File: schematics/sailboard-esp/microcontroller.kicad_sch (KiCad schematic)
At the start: 2 parts

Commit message: v1.1 of sailboard.
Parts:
- removed LOGICTRANS1: TXB0108DQSR, Package_SON:USON-20_2x4mm_P0.4mm, symbol Logic_LevelTranslator:TXB0108DQSR
- added LEVEL_TRANSLATE1: TXB0108PWR, SOP65P640X120-20N, symbol TXB0108PWR:TXB0108PWR
- ESP32: footprint MODULE_ESP32-DEVKITC -> ESP32-DEVKITC:MODULE_ESP32-DEVKITC-RESIZED
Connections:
- net +3.3V: now also LEVEL_TRANSLATE1.10 (OE), LEVEL_TRANSLATE1.2 (VCCA)
- net +5V: now also LEVEL_TRANSLATE1.19 (VCCB)
- net GND: now also LEVEL_TRANSLATE1.11 (GND)
- net PROP_ENABLE_1_5V: now also LEVEL_TRANSLATE1.18 (B2)
- net PROP_ENABLE_2_5V: now also LEVEL_TRANSLATE1.20 (B1)
- net PROP_PWM_5V: now also LEVEL_TRANSLATE1.17 (B3)
- net RADIO_CHAN1_5V: now also LEVEL_TRANSLATE1.15 (B5)
- net RADIO_CHAN2_5V: now also LEVEL_TRANSLATE1.14 (B6)
- net RUDDER_PWM_5V: now also LEVEL_TRANSLATE1.16 (B4)
- net at ESP32.28 (IO17): now also LEVEL_TRANSLATE1.1 (A1)
- net at ESP32.27 (IO16): now also LEVEL_TRANSLATE1.3 (A2)
- net at ESP32.26 (IO4): now also LEVEL_TRANSLATE1.4 (A3)
- net at ESP32.25 (IO0): now also LEVEL_TRANSLATE1.5 (A4)
- net at ESP32.24 (IO2): now also LEVEL_TRANSLATE1.6 (A5)
- net at ESP32.23 (IO15): now also LEVEL_TRANSLATE1.7 (A6)

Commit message: move to version 1.2.
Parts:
- removed LEVEL_TRANSLATE1: TXB0108PWR, SOP65P640X120-20N, symbol TXB0108PWR:TXB0108PWR
- added IC1: TXB0108PWR, SOP65P640X120-20N, symbol TXB0108PWR:TXB0108PWR
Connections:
- net +3.3V: now also IC1.10 (OE), IC1.2 (VCCA)
- net +5V: now also IC1.19 (VCCB)
- net GND: now also IC1.11 (GND)
- net IRIDIUM_SLEEP: now also ESP32.6 (IO35); no longer ESP32.8 (IO33)
- net PROP_ENABLE_1_5V: now also IC1.18 (B2)
- net PROP_ENABLE_2_5V: now also IC1.20 (B1)
- net PROP_PWM_5V: now also IC1.17 (B3)
- net RADIO_CHAN1_5V: now also IC1.15 (B5)
- net RADIO_CHAN2_5V: now also IC1.14 (B6)
- net RUDDER_PWM_5V: now also IC1.16 (B4)
- net ARDUCAM_CS: now reaches ESP32.10 (IO26)
- net SDCARD_SCK: now reaches ESP32.12 (IO14)
- net SDCARD_D2: now reaches ESP32.13 (IO12)
- net SDCARD_D3: now reaches ESP32.15 (IO13)
- net SDCARD_CMD: now reaches ESP32.23 (IO15)
- net SDCARD_D0: now reaches ESP32.24 (IO2)
- net at ESP32.25 (IO0): now also IC1.4 (A3)
- net SDCARD_D1: now reaches ESP32.26 (IO4)
- net at ESP32.27 (IO16): now also IC1.3 (A2)
- net at ESP32.28 (IO17): now also IC1.1 (A1)
- net RUDDER_PWM: now reaches ESP32.5 (IO34)
- net RUDDER_PWM: now also IC1.5 (A4)
- net RADIO_CHAN2: now reaches ESP32.9 (IO25)
- net RADIO_CHAN2: now also IC1.7 (A6)
- new net RADIO_CHAN1: ESP32.8 (IO33), IC1.6 (A5)
- no-connect marks 21 -> 14

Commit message: v1.3.
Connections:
- net PROP_PWM: now reaches ESP32.11 (IO27)
- net PROP_PWM: now also IC1.4 (A3)
- net at ESP32.25 (IO0): no longer IC1.4 (A3)
- no-connect marks 14 -> 15
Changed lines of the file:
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@@
 (kicad_sch (version 20211123) (generator eeschema)
   (paper "A4")
-  (no_connect (at 106.68 76.2))
   (no_connect (at 106.68 53.34))
   (no_connect (at 106.68 93.98))
@@
   (no_connect (at 106.68 58.42))
   (no_connect (at 106.68 50.8))
+  (no_connect (at 147.32 83.82))
+  (no_connect (at 134.62 74.295))
   (no_connect (at 203.2 91.44))
   (no_connect (at 203.2 93.98))
@@
     (stroke (width 0) (type default) (color 0 0 0 0))
   )
-  (wire (pts (xy 95.25 73.66) (xy 106.68 73.66))
+  (wire (pts (xy 90.17 73.66) (xy 106.68 73.66))
     (stroke (width 0) (type default) (color 0 0 0 0))
   )
@@
     (stroke (width 0) (type default) (color 0 0 0 0))
   )
-  (wire (pts (xy 147.32 83.82) (xy 184.15 83.82))
-    (stroke (width 0) (type default) (color 0 0 0 0))
-  )
-  (wire (pts (xy 184.15 83.82) (xy 184.15 81.28))
-    (stroke (width 0) (type default) (color 0 0 0 0))
-  )
   (wire (pts (xy 170.18 76.2) (xy 147.32 76.2))
     (stroke (width 0) (type default) (color 0 0 0 0))
@@
     (stroke (width 0) (type default) (color 0 0 0 0))
   )
+  (wire (pts (xy 95.25 76.2) (xy 106.68 76.2))
+    (stroke (width 0) (type default) (color 0 0 0 0))
+  )
   (wire (pts (xy 81.28 68.58) (xy 106.68 68.58))
     (stroke (width 0) (type default) (color 0 0 0 0))
@@
     (stroke (width 0) (type default) (color 0 0 0 0))
   )
-  (wire (pts (xy 184.15 81.28) (xy 203.2 81.28))
+  (wire (pts (xy 187.96 81.28) (xy 203.2 81.28))
     (stroke (width 0) (type default) (color 0 0 0 0))
   )
@@
     (effects (font (size 1.27 1.27)) (justify left bottom))
   )
+  (label "PROP_PWM" (at 187.96 81.28 0)
+    (effects (font (size 1.27 1.27)) (justify left bottom))
+  )
   (label "RADIO_CHAN2" (at 187.96 88.9 0)
     (effects (font (size 1.27 1.27)) (justify left bottom))
@@
     (effects (font (size 1.27 1.27)) (justify left bottom))
   )
+  (label "PROP_PWM" (at 95.25 76.2 0)
+    (effects (font (size 1.27 1.27)) (justify left bottom))
+  )
   (label "RUDDER_PWM" (at 187.96 83.82 0)
     (effects (font (size 1.27 1.27)) (justify left bottom))
@@
     (effects (font (size 1.27 1.27)) (justify right))
   )
-  (hierarchical_label "ARDUCAM_CS" (shape input) (at 95.25 73.66 180)
-    (effects (font (size 1.27 1.27)) (justify right))
-  )
+  (hierarchical_label "ARDUCAM_CS" (shape input) (at 90.17 73.66 180)
+    (effects (font (size 1.27 1.27)) (justify right))
+  )

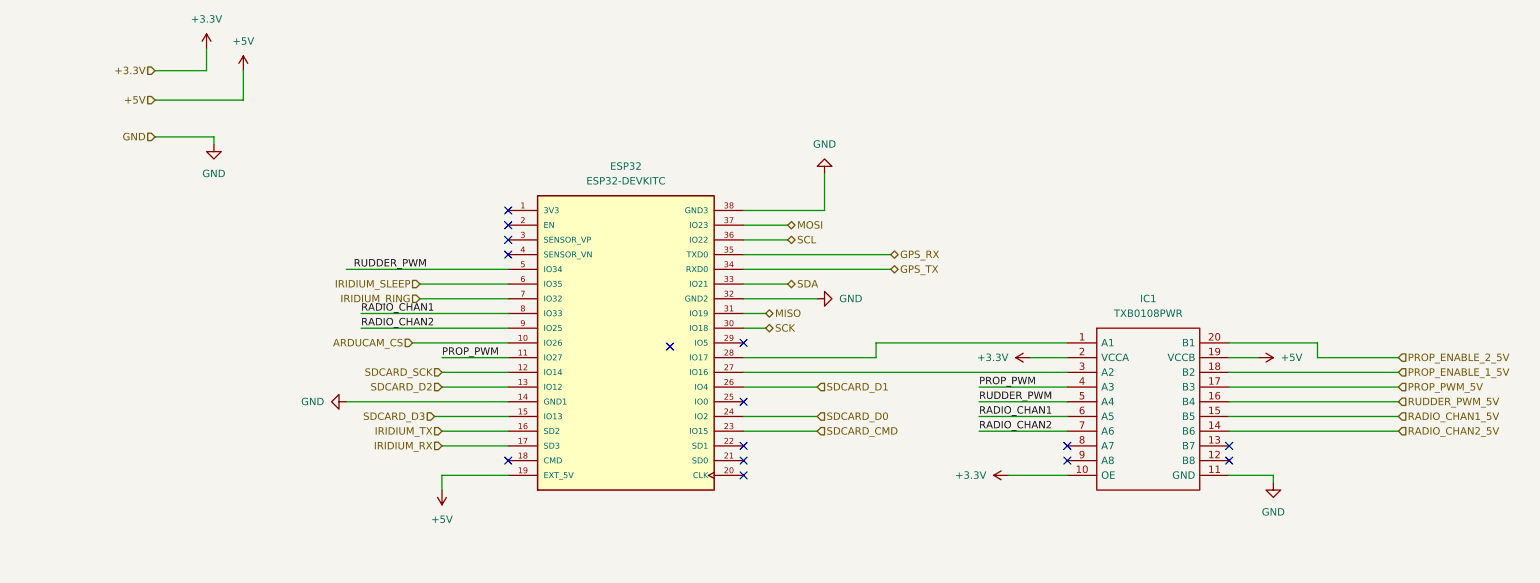
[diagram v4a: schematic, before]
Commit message: rearrange pins to avoid ESP32 reserved / wonky pins.
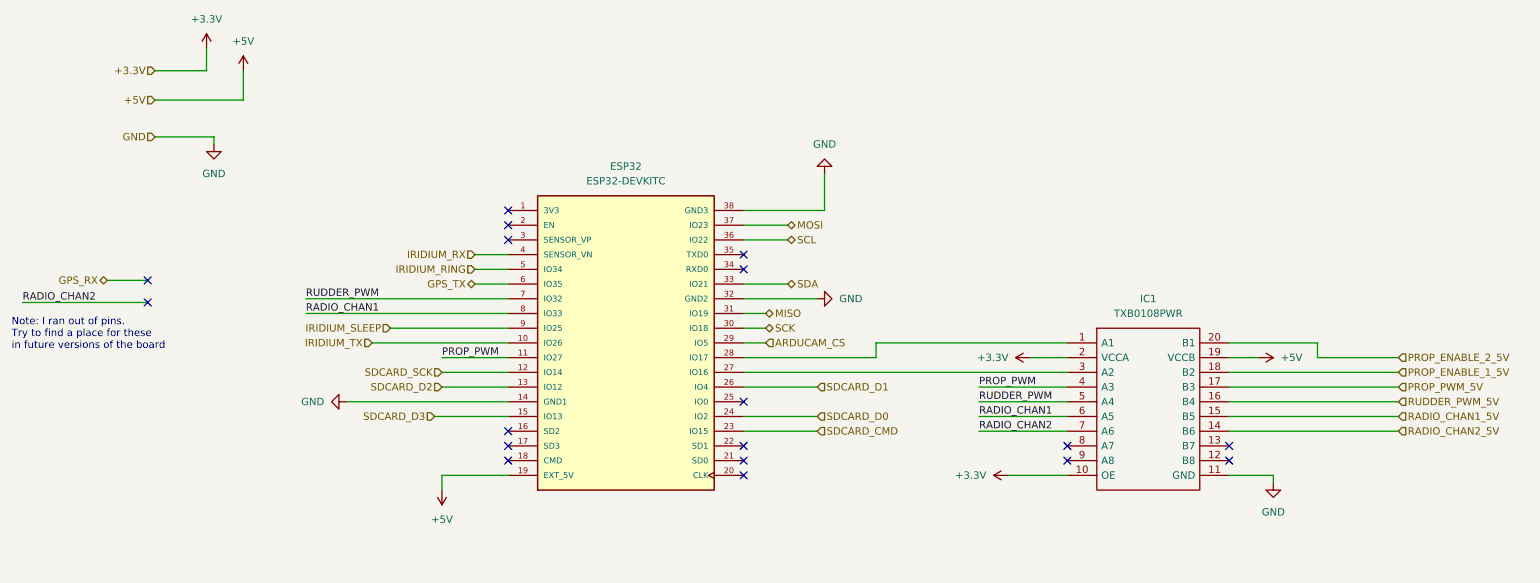
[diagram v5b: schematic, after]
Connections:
- net ARDUCAM_CS: now also ESP32.29 (IO5); no longer ESP32.10 (IO26)
- net GPS_RX: no longer ESP32.35 (TXD0)
- net GPS_TX: now also ESP32.6 (IO35); no longer ESP32.34 (RXD0)
- net IRIDIUM_RING: now also ESP32.5 (IO34); no longer ESP32.7 (IO32)
- net IRIDIUM_RX: now also ESP32.4 (SENSOR_VN); no longer ESP32.17 (SD3)
- net IRIDIUM_SLEEP: now also ESP32.9 (IO25); no longer ESP32.6 (IO35)
- net IRIDIUM_TX: now also ESP32.10 (IO26); no longer ESP32.16 (SD2)
- net RADIO_CHAN2: no longer ESP32.9 (IO25)
- net RUDDER_PWM: now also ESP32.7 (IO32); no longer ESP32.5 (IO34)
- no-connect marks 15 -> 18
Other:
- note added: "Note: I ran out of pins. Try to find a place for these in future versions of the board"
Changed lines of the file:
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@@
 (kicad_sch (version 20211123) (generator eeschema)
   (paper "A4")
+  (no_connect (at 147.32 58.42))
+  (no_connect (at 147.32 60.96))
   (no_connect (at 106.68 53.34))
   (no_connect (at 106.68 93.98))
-  (no_connect (at 147.32 73.66))
   (no_connect (at 147.32 91.44))
   (no_connect (at 147.32 93.98))
   (no_connect (at 147.32 96.52))
   (no_connect (at 106.68 55.88))
-  (no_connect (at 106.68 58.42))
   (no_connect (at 106.68 50.8))
   (no_connect (at 147.32 83.82))
-  (no_connect (at 134.62 74.295))
+  (no_connect (at 106.68 91.44))
+  (no_connect (at 106.68 88.9))
+  (no_connect (at 44.45 66.675))
   (no_connect (at 203.2 91.44))
   (no_connect (at 203.2 93.98))
   (no_connect (at 231.14 91.44))
   (no_connect (at 231.14 93.98))
+  (no_connect (at 44.45 62.865))
   (wire (pts (xy 147.32 81.28) (xy 160.02 81.28))
     (stroke (width 0) (type default) (color 0 0 0 0))
@@
     (stroke (width 0) (type default) (color 0 0 0 0))
   )
+  (wire (pts (xy 83.185 73.66) (xy 106.68 73.66))
+    (stroke (width 0) (type default) (color 0 0 0 0))
+  )
   (wire (pts (xy 231.14 73.66) (xy 246.38 73.66))
     (stroke (width 0) (type default) (color 0 0 0 0))
@@
     (stroke (width 0) (type default) (color 0 0 0 0))
   )
+  (wire (pts (xy 37.465 62.865) (xy 44.45 62.865))
+    (stroke (width 0) (type default) (color 0 0 0 0))
+  )
+  (wire (pts (xy 22.86 66.675) (xy 44.45 66.675))
+    (stroke (width 0) (type default) (color 0 0 0 0))
+  )
   (wire (pts (xy 193.04 96.52) (xy 203.2 96.52))
     (stroke (width 0) (type default) (color 0 0 0 0))
   )
-  (wire (pts (xy 147.32 58.42) (xy 172.72 58.42))
-    (stroke (width 0) (type default) (color 0 0 0 0))
-  )
-  (wire (pts (xy 95.25 91.44) (xy 106.68 91.44))
+  (wire (pts (xy 71.755 66.04) (xy 106.68 66.04))
     (stroke (width 0) (type default) (color 0 0 0 0))
   )
@@
     (stroke (width 0) (type default) (color 0 0 0 0))
   )
-  (wire (pts (xy 95.25 88.9) (xy 106.68 88.9))
-    (stroke (width 0) (type default) (color 0 0 0 0))
-  )
   (wire (pts (xy 231.14 83.82) (xy 260.35 83.82))
     (stroke (width 0) (type default) (color 0 0 0 0))
@@
     (stroke (width 0) (type default) (color 0 0 0 0))
   )
-  (wire (pts (xy 91.44 66.04) (xy 106.68 66.04))
-    (stroke (width 0) (type default) (color 0 0 0 0))
-  )
-  (wire (pts (xy 90.17 73.66) (xy 106.68 73.66))
-    (stroke (width 0) (type default) (color 0 0 0 0))
-  )
   (wire (pts (xy 231.14 81.28) (xy 260.35 81.28))
     (stroke (width 0) (type default) (color 0 0 0 0))
@@
     (stroke (width 0) (type default) (color 0 0 0 0))
   )
-  (wire (pts (xy 91.44 63.5) (xy 106.68 63.5))
+  (wire (pts (xy 86.36 71.12) (xy 106.68 71.12))
+    (stroke (width 0) (type default) (color 0 0 0 0))
+  )
+  (wire (pts (xy 100.965 60.96) (xy 106.68 60.96))
     (stroke (width 0) (type default) (color 0 0 0 0))
   )
@@
     (stroke (width 0) (type default) (color 0 0 0 0))
   )
-  (wire (pts (xy 147.32 60.96) (xy 172.72 60.96))
+  (wire (pts (xy 147.32 73.66) (xy 151.13 73.66))
     (stroke (width 0) (type default) (color 0 0 0 0))
   )
@@
     (stroke (width 0) (type default) (color 0 0 0 0))
   )
-  (wire (pts (xy 78.74 60.96) (xy 106.68 60.96))
-    (stroke (width 0) (type default) (color 0 0 0 0))
-  )
   (wire (pts (xy 238.76 96.52) (xy 238.76 97.79))
     (stroke (width 0) (type default) (color 0 0 0 0))
   )
-  (wire (pts (xy 81.28 71.12) (xy 106.68 71.12))
-    (stroke (width 0) (type default) (color 0 0 0 0))
-  )
   (wire (pts (xy 95.25 99.06) (xy 95.25 96.52))
     (stroke (width 0) (type default) (color 0 0 0 0))
@@
     (stroke (width 0) (type default) (color 0 0 0 0))
   )
-  (wire (pts (xy 81.28 68.58) (xy 106.68 68.58))
+  (wire (pts (xy 71.755 68.58) (xy 106.68 68.58))
     (stroke (width 0) (type default) (color 0 0 0 0))
   )
@@
     (stroke (width 0) (type default) (color 0 0 0 0))
   )
+  (wire (pts (xy 100.965 58.42) (xy 106.68 58.42))
+    (stroke (width 0) (type default) (color 0 0 0 0))
+  )
   (wire (pts (xy 231.14 86.36) (xy 260.35 86.36))
     (stroke (width 0) (type default) (color 0 0 0 0))
   )
+  (wire (pts (xy 100.965 63.5) (xy 106.68 63.5))
+    (stroke (width 0) (type default) (color 0 0 0 0))
+  )
   (wire (pts (xy 161.29 50.8) (xy 161.29 44.45))
     (stroke (width 0) (type default) (color 0 0 0 0))
@@
     (stroke (width 0) (type default) (color 0 0 0 0))
   )
-  (label "RADIO_CHAN2" (at 81.28 71.12 0)
+  (text "Note: I ran out of pins. \nTry to find a place for these \nin future versions of the board"
+    (at 20.955 74.93 0)
     (effects (font (size 1.27 1.27)) (justify left bottom))
   )
@@
     (effects (font (size 1.27 1.27)) (justify left bottom))
   )
-  (label "RADIO_CHAN1" (at 81.28 68.58 0)
+  (label "RADIO_CHAN1" (at 71.755 68.58 0)
+    (effects (font (size 1.27 1.27)) (justify left bottom))
+  )
+  (label "RUDDER_PWM" (at 71.755 66.04 0)
     (effects (font (size 1.27 1.27)) (justify left bottom))
   )
@@
     (effects (font (size 1.27 1.27)) (justify left bottom))
   )
-  (label "RUDDER_PWM" (at 80.01 60.96 0)
+  (label "RADIO_CHAN2" (at 22.86 66.675 0)
     (effects (font (size 1.27 1.27)) (justify left bottom))
   )
@@
     (effects (font (size 1.27 1.27)) (justify right))
   )
-  (hierarchical_label "GPS_TX" (shape bidirectional) (at 172.72 60.96 0)
-    (effects (font (size 1.27 1.27)) (justify left))
+  (hierarchical_label "GPS_TX" (shape bidirectional) (at 100.965 63.5 180)
+    (effects (font (size 1.27 1.27)) (justify right))
   )
   (hierarchical_label "SDA" (shape bidirectional) (at 154.94 63.5 0)
@@
     (effects (font (size 1.27 1.27)) (justify left))
   )
-  (hierarchical_label "IRIDIUM_TX" (shape input) (at 95.25 88.9 180)
+  (hierarchical_label "IRIDIUM_TX" (shape input) (at 83.185 73.66 180)
     (effects (font (size 1.27 1.27)) (justify right))
   )
@@
     (effects (font (size 1.27 1.27)) (justify right))
   )
-  (hierarchical_label "IRIDIUM_SLEEP" (shape input) (at 91.44 63.5 180)
-    (effects (font (size 1.27 1.27)) (justify right))
-  )
-  (hierarchical_label "GPS_RX" (shape bidirectional) (at 172.72 58.42 0)
-    (effects (font (size 1.27 1.27)) (justify left))
+  (hierarchical_label "IRIDIUM_SLEEP" (shape input) (at 86.36 71.12 180)
+    (effects (font (size 1.27 1.27)) (justify right))
+  )
+  (hierarchical_label "GPS_RX" (shape bidirectional) (at 37.465 62.865 180)
+    (effects (font (size 1.27 1.27)) (justify right))
   )
   (hierarchical_label "SDCARD_CMD" (shape input) (at 160.02 88.9 0)
@@
     (effects (font (size 1.27 1.27)) (justify right))
   )
-  (hierarchical_label "IRIDIUM_RX" (shape input) (at 95.25 91.44 180)
-    (effects (font (size 1.27 1.27)) (justify right))
-  )
-  (hierarchical_label "ARDUCAM_CS" (shape input) (at 90.17 73.66 180)
-    (effects (font (size 1.27 1.27)) (justify right))
+  (hierarchical_label "IRIDIUM_RX" (shape input) (at 100.965 58.42 180)
+    (effects (font (size 1.27 1.27)) (justify right))
+  )
+  (hierarchical_label "ARDUCAM_CS" (shape input) (at 151.13 73.66 0)
+    (effects (font (size 1.27 1.27)) (justify left))
   )
   (hierarchical_label "PROP_ENABLE_1_5V" (shape input) (at 260.35 78.74 0)
@@
     (effects (font (size 1.27 1.27)) (justify left))
   )
-  (hierarchical_label "IRIDIUM_RING" (shape input) (at 91.44 66.04 180)
-    (effects (font (size 1.27 1.27)) (justify right))
-  )
+  (hierarchical_label "IRIDIUM_RING" (shape input) (at 100.965 60.96 180)
+    (effects (font (size 1.27 1.27)) (justify right))
+  )
